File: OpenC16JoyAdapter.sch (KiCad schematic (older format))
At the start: 16 parts, among them J1 DB9_MALE, J2 TO_C16_MINI_DIN_8, Q1 BC548, Q2 BC547, Q3 BC547, SW1 SW_PIN5_POWER, SW2 SW_LIGHTPEN, U1 74LS244

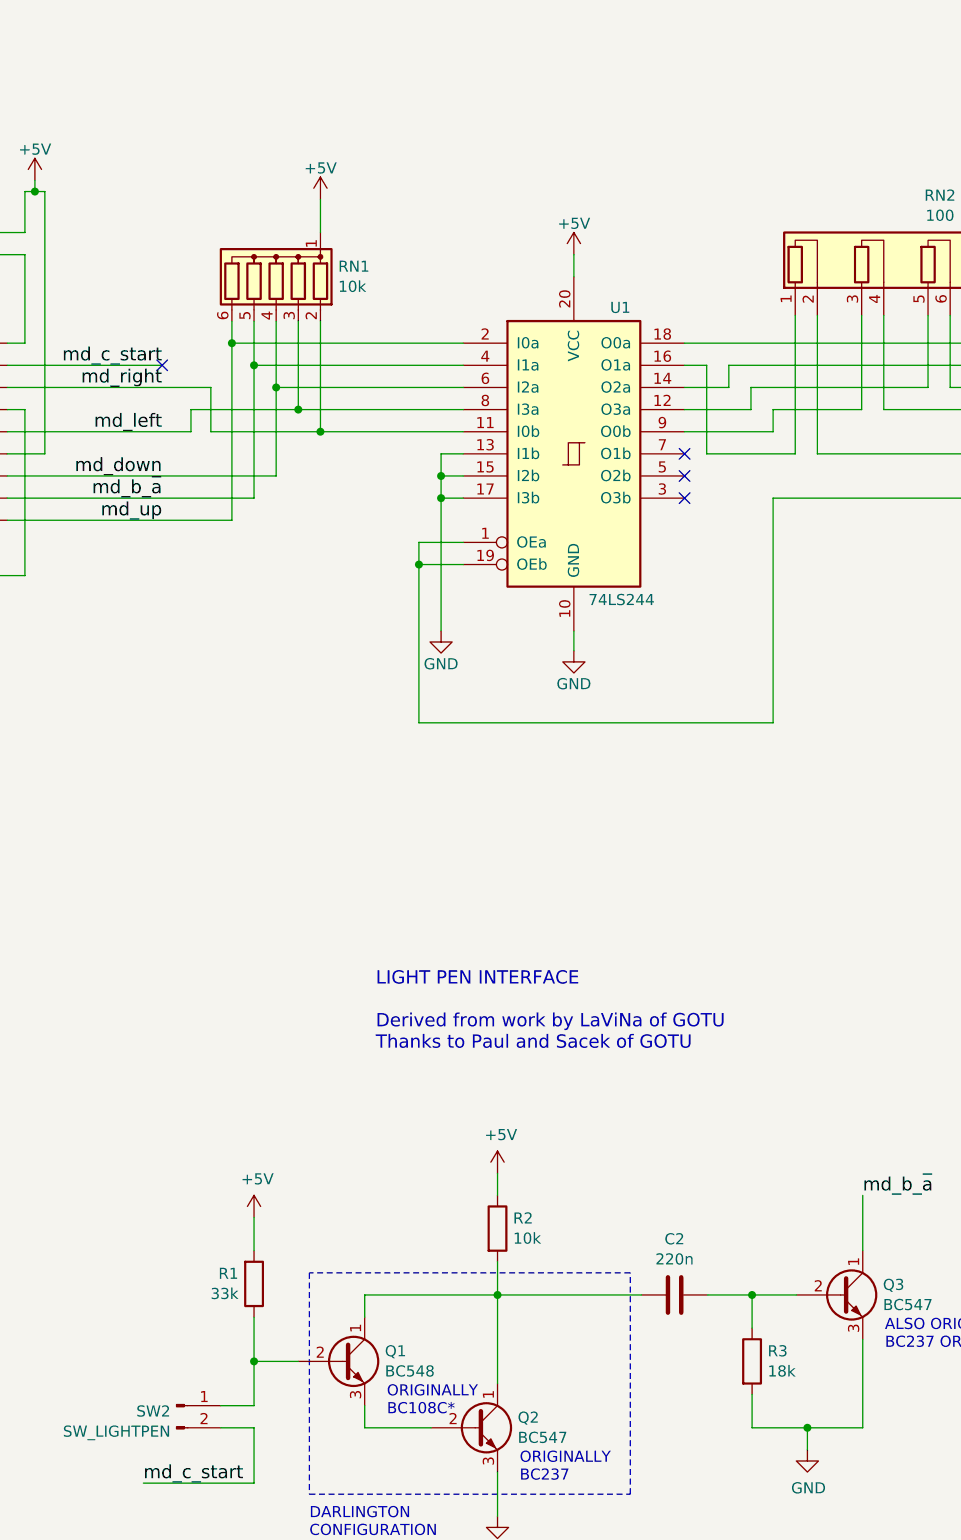
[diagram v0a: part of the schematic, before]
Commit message: Add light pen circuit to PCB
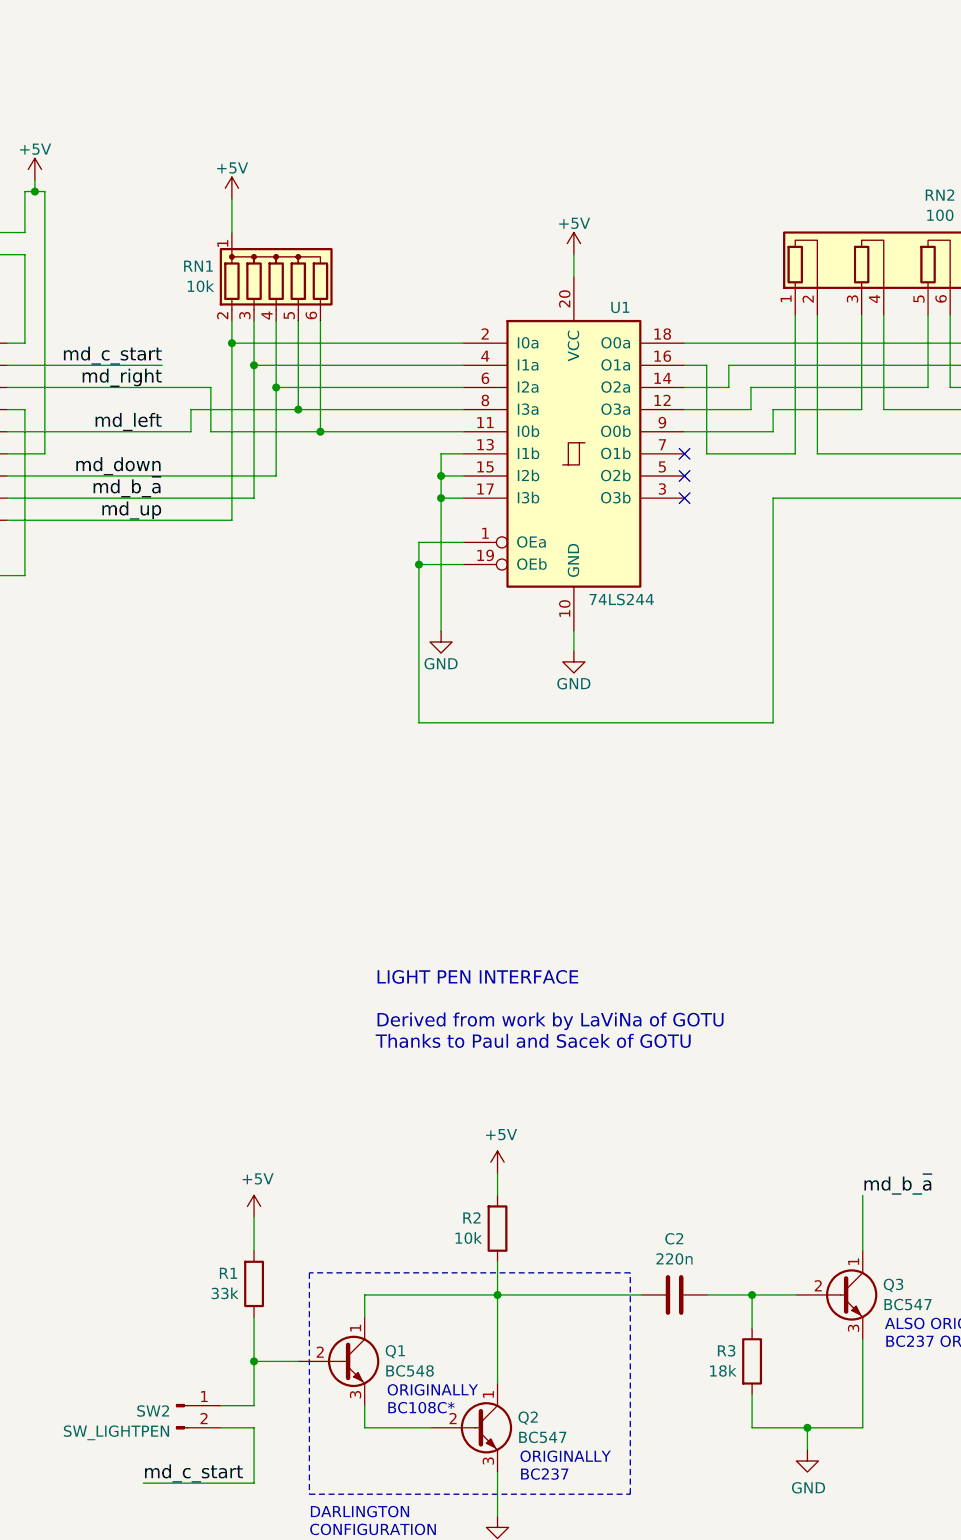
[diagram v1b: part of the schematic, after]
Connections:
- net +5V: now also R2.2; no longer R2.1
- net md_b_~a: now also RN1.3 (R2); no longer RN1.5 (R4)
- net md_left: now also RN1.5 (R4); no longer RN1.3 (R2)
- net md_right: now also RN1.6 (R5); no longer RN1.2 (R1)
- net md_up: now also RN1.2 (R1); no longer RN1.6 (R5)
- net at C2.2, Q1.1 (C), Q2.1 (C): now also R2.1; no longer R2.2
- no-connect marks 4 -> 3
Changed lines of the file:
@@
 Comment1 "http://www.commodore.ca/manuals/funet/cbm/documents/projects/interfaces/plus4joy/plus4joy.html"
 Comment2 "Based on work by Levente Hársfalvi (TLC)"
-Comment3 "Licensed under CERN OHL v.1.2"
-Comment4 ""
+Comment3 "Light pen circuit by LaViNa, Paul and Sacek of GOTU"
+Comment4 "Licensed under CERN OHL v.1.2"
 $EndDescr
 $Comp
@@
 Text Label 5835 2700 2    60   ~ 0
 md_c_start
-NoConn ~ 5835 2700
 Text Notes 5015 1990 2    60   ~ 0
 Short for Sega Mega\nDrive controllers, leave\nopen otherwise
@@
 	0    1    1    0
 $EndComp
-$Comp
-L Device:R_Network05 RN1
-U 1 1 5A45976E
-P 6350 2300
-F 0 "RN1" H 6070 2346 50  0000 R CNN
-F 1 "10k" H 6070 2255 50  0000 R CNN
-F 2 "Resistor_THT:R_Array_SIP6" V 6725 2300 50  0001 C CNN
-F 3 "" H 6350 2300 50  0001 C CNN
-	1    6350 2300
-	-1   0    0    -1
-$EndComp
 Wire Wire Line
 	7095 3200 7195 3200
@@
 	6250 2700 7195 2700
 Wire Wire Line
-	6550 1950 6550 2100
+	6150 1950 6150 2100
 $Comp
 L power:+5V #PWR0101
 U 1 1 65B61C22
-P 6550 1950
-F 0 "#PWR0101" H 6550 1800 50  0001 C CNN
-F 1 "+5V" H 6550 2090 50  0000 C CNN
-F 2 "" H 6550 1950 50  0000 C CNN
-F 3 "" H 6550 1950 50  0000 C CNN
-	1    6550 1950
+P 6150 1950
+F 0 "#PWR0101" H 6150 1800 50  0001 C CNN
+F 1 "+5V" H 6150 2090 50  0000 C CNN
+F 2 "" H 6150 1950 50  0000 C CNN
+F 3 "" H 6150 1950 50  0000 C CNN
+	1    6150 1950
 	1    0    0    -1
 $EndComp
@@
 $Comp
 L Device:R R?
-U 1 1 66E70DD1
-P 7350 6600
-AR Path="/66E4FBCD/66E70DD1" Ref="R?"  Part="1"
-AR Path="/66E70DD1" Ref="R2"  Part="1"
-F 0 "R2" H 7420 6646 50  0000 L CNN
-F 1 "10k" H 7420 6555 50  0000 L CNN
-F 2 "Resistor_THT:R_Axial_DIN0207_L6.3mm_D2.5mm_P2.54mm_Vertical" V 7280 6600 50  0001 C CNN
-F 3 "~" H 7350 6600 50  0001 C CNN
-	1    7350 6600
-	1    0    0    -1
-$EndComp
-$Comp
-L Device:R R?
 U 1 1 66E70DD7
 P 8500 7200
 AR Path="/66E4FBCD/66E70DD7" Ref="R?"  Part="1"
 AR Path="/66E70DD7" Ref="R3"  Part="1"
-F 0 "R3" H 8570 7246 50  0000 L CNN
-F 1 "18k" H 8570 7155 50  0000 L CNN
+F 0 "R3" H 8430 7246 50  0000 R CNN
+F 1 "18k" H 8430 7155 50  0000 R CNN
 F 2 "Resistor_THT:R_Axial_DIN0207_L6.3mm_D2.5mm_P2.54mm_Vertical" V 8430 7200 50  0001 C CNN
 F 3 "~" H 8500 7200 50  0001 C CNN
@@
 Text Label 9000 6450 0    60   ~ 0
 md_b_~a
+$Comp
+L Device:R R?
+U 1 1 66E70DD1
+P 7350 6600
+AR Path="/66E4FBCD/66E70DD1" Ref="R?"  Part="1"
+AR Path="/66E70DD1" Ref="R2"  Part="1"
+F 0 "R2" H 7280 6554 50  0000 R CNN
+F 1 "10k" H 7280 6645 50  0000 R CNN
+F 2 "Resistor_THT:R_Axial_DIN0207_L6.3mm_D2.5mm_P2.54mm_Vertical" V 7280 6600 50  0001 C CNN
+F 3 "~" H 7350 6600 50  0001 C CNN
+	1    7350 6600
+	1    0    0    1
+$EndComp
+$Comp
+L Device:R_Network05 RN1
+U 1 1 5A45976E
+P 6350 2300
+F 0 "RN1" H 6070 2346 50  0000 R CNN
+F 1 "10k" H 6070 2255 50  0000 R CNN
+F 2 "Resistor_THT:R_Array_SIP6" V 6725 2300 50  0001 C CNN
+F 3 "" H 6350 2300 50  0001 C CNN
+	1    6350 2300
+	1    0    0    -1
+$EndComp
 $EndSCHEMATC
